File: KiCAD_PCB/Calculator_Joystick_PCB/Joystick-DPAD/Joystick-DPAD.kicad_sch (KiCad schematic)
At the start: 2 parts

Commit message: Updated Joystick PCB
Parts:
- gave numbers to parts that had none: 1
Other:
- moved on the sheet: JOY1A, JOY1B
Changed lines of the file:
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@@
     (title "Joystick & D-PAD Module")
   )
-  (wire (pts (xy 39.116 21.844) (xy 39.116 24.384))
+  (wire (pts (xy 28.956 27.432) (xy 28.956 29.972))
     (stroke (width 0) (type default) (color 0 0 0 0))
   )
-  (wire (pts (xy 44.45 51.562) (xy 46.99 51.562))
+  (wire (pts (xy 34.29 57.15) (xy 36.83 57.15))
     (stroke (width 0) (type default) (color 0 0 0 0))
   )
-  (wire (pts (xy 44.196 29.464) (xy 46.99 29.464))
+  (wire (pts (xy 34.036 35.052) (xy 36.83 35.052))
     (stroke (width 0) (type default) (color 0 0 0 0))
   )
-  (label "XOUT" (at 46.99 29.464 0)
+  (label "XOUT" (at 36.83 35.052 0)
     (effects (font (size 1.2446 1.2446)) (justify left bottom))
   )
-  (label "YOUT" (at 46.99 51.562 0)
+  (label "YOUT" (at 36.83 57.15 0)
     (effects (font (size 1.2446 1.2446)) (justify left bottom))
   )
-  (symbol (lib_id "Adafruit Mini Analog Thumbstick-eagle-import:GND") (at 39.116 37.084 0) (mirror y) (unit 1)
+  (symbol (lib_id "Adafruit Mini Analog Thumbstick-eagle-import:GND") (at 28.956 42.672 0) (mirror y) (unit 1)
     (in_bom yes) (on_board yes)
-    (property "Reference" "#GND?" (id 0) (at 39.116 37.084 0)
+    (property "Reference" "#GND0102" (id 0) (at 28.956 42.672 0)
       (effects (font (size 1.27 1.27)) hide)
     )
-    (property "Value" "GND" (id 1) (at 41.656 39.624 0)
+    (property "Value" "GND" (id 1) (at 31.496 45.212 0)
       (effects (font (size 1.778 1.5113)) (justify left bottom))
     )
-    (property "Footprint" "Adafruit Mini Analog Thumbstick:" (id 2) (at 39.116 37.084 0)
+    (property "Footprint" "Adafruit Mini Analog Thumbstick:" (id 2) (at 28.956 42.672 0)
       (effects (font (size 1.27 1.27)) hide)
     )
-    (property "Datasheet" "" (id 3) (at 39.116 37.084 0)
+    (property "Datasheet" "" (id 3) (at 28.956 42.672 0)
       (effects (font (size 1.27 1.27)) hide)
     )
     (pin "1")
   )
-  (symbol (lib_id "Adafruit Mini Analog Thumbstick-eagle-import:GND") (at 39.37 59.182 0) (mirror y) (unit 1)
+  (symbol (lib_id "Adafruit Mini Analog Thumbstick-eagle-import:GND") (at 29.21 64.77 0) (mirror y) (unit 1)
     (in_bom yes) (on_board yes)
-    (property "Reference" "#GND?" (id 0) (at 39.37 59.182 0)
+    (property "Reference" "#GND0101" (id 0) (at 29.21 64.77 0)
       (effects (font (size 1.27 1.27)) hide)
     )
-    (property "Value" "GND" (id 1) (at 41.91 61.722 0)
+    (property "Value" "GND" (id 1) (at 31.75 67.31 0)
       (effects (font (size 1.778 1.5113)) (justify left bottom))
     )
-    (property "Footprint" "Adafruit Mini Analog Thumbstick:" (id 2) (at 39.37 59.182 0)
+    (property "Footprint" "Adafruit Mini Analog Thumbstick:" (id 2) (at 29.21 64.77 0)
       (effects (font (size 1.27 1.27)) hide)
     )
-    (property "Datasheet" "" (id 3) (at 39.37 59.182 0)
+    (property "Datasheet" "" (id 3) (at 29.21 64.77 0)
       (effects (font (size 1.27 1.27)) hide)
     )
     (pin "1")
   )
-  (symbol (lib_id "Adafruit Mini Analog Thumbstick-eagle-import:JOYSTICK_ANALOG_XY") (at 39.116 29.464 0) (unit 1)
+  (symbol (lib_id "Adafruit Mini Analog Thumbstick-eagle-import:JOYSTICK_ANALOG_XY") (at 28.956 35.052 0) (unit 1)
     (in_bom yes) (on_board yes)
-    (property "Reference" "JOY?" (id 0) (at 33.147 33.274 90)
+    (property "Reference" "JOY1" (id 0) (at 22.987 38.862 90)
       (effects (font (size 1.27 1.0795)) (justify left bottom))
     )
-    (property "Value" "JOYSTICK_ANALOG_XY" (id 1) (at 35.306 33.274 90)
+    (property "Value" "JOYSTICK_ANALOG_XY" (id 1) (at 25.146 38.862 90)
       (effects (font (size 1.27 1.0795)) (justify left bottom))
     )
-    (property "Footprint" "Adafruit Mini Analog Thumbstick:JOYSTICK_ANALOG_MINITHM" (id 2) (at 39.116 29.464 0)
+    (property "Footprint" "Adafruit Mini Analog Thumbstick:JOYSTICK_ANALOG_MINITHM" (id 2) (at 28.956 35.052 0)
       (effects (font (size 1.27 1.27)) hide)
     )
-    (property "Datasheet" "" (id 3) (at 39.116 29.464 0)
+    (property "Datasheet" "" (id 3) (at 28.956 35.052 0)
       (effects (font (size 1.27 1.27)) hide)
     )
@@
     (pin "Y-")
   )
-  (symbol (lib_id "Adafruit Mini Analog Thumbstick-eagle-import:3.3V") (at 39.37 43.942 0) (unit 1)
+  (symbol (lib_id "Adafruit Mini Analog Thumbstick-eagle-import:3.3V") (at 29.21 49.53 0) (unit 1)
     (in_bom yes) (on_board yes)
-    (property "Reference" "#U$?" (id 0) (at 39.37 43.942 0)
+    (property "Reference" "#U$0101" (id 0) (at 29.21 49.53 0)
       (effects (font (size 1.27 1.27)) hide)
     )
-    (property "Value" "3.3V" (id 1) (at 37.846 42.926 0)
+    (property "Value" "3.3V" (id 1) (at 27.686 48.514 0)
       (effects (font (size 1.27 1.0795)) (justify left bottom))
     )
-    (property "Footprint" "Adafruit Mini Analog Thumbstick:" (id 2) (at 39.37 43.942 0)
+    (property "Footprint" "Adafruit Mini Analog Thumbstick:" (id 2) (at 29.21 49.53 0)
       (effects (font (size 1.27 1.27)) hide)
     )
-    (property "Datasheet" "" (id 3) (at 39.37 43.942 0)
+    (property "Datasheet" "" (id 3) (at 29.21 49.53 0)
       (effects (font (size 1.27 1.27)) hide)
     )
     (pin "1")
   )
-  (symbol (lib_id "Adafruit Mini Analog Thumbstick-eagle-import:JOYSTICK_ANALOG_XY") (at 39.37 51.562 0) (unit 2)
+  (symbol (lib_id "Adafruit Mini Analog Thumbstick-eagle-import:JOYSTICK_ANALOG_XY") (at 29.21 57.15 0) (unit 2)
     (in_bom yes) (on_board yes)
-    (property "Reference" "JOY?" (id 0) (at 33.401 55.372 90)
+    (property "Reference" "JOY1" (id 0) (at 23.241 60.96 90)
       (effects (font (size 1.27 1.0795)) (justify left bottom))
     )
-    (property "Value" "JOYSTICK_ANALOG_XY" (id 1) (at 35.56 55.372 90)
+    (property "Value" "JOYSTICK_ANALOG_XY" (id 1) (at 25.4 60.96 90)
       (effects (font (size 1.27 1.0795)) (justify left bottom))
     )
-    (property "Footprint" "Adafruit Mini Analog Thumbstick:JOYSTICK_ANALOG_MINITHM" (id 2) (at 39.37 51.562 0)
+    (property "Footprint" "Adafruit Mini Analog Thumbstick:JOYSTICK_ANALOG_MINITHM" (id 2) (at 29.21 57.15 0)
       (effects (font (size 1.27 1.27)) hide)
     )
-    (property "Datasheet" "" (id 3) (at 39.37 51.562 0)
+    (property "Datasheet" "" (id 3) (at 29.21 57.15 0)
       (effects (font (size 1.27 1.27)) hide)
     )
@@
     (pin "Y-")
   )
-  (symbol (lib_id "Adafruit Mini Analog Thumbstick-eagle-import:3.3V") (at 39.116 19.304 0) (unit 1)
+  (symbol (lib_id "Adafruit Mini Analog Thumbstick-eagle-import:3.3V") (at 28.956 24.892 0) (unit 1)
     (in_bom yes) (on_board yes)
-    (property "Reference" "#U$?" (id 0) (at 39.116 19.304 0)
+    (property "Reference" "#U$0102" (id 0) (at 28.956 24.892 0)
       (effects (font (size 1.27 1.27)) hide)
     )
-    (property "Value" "3.3V" (id 1) (at 37.592 18.288 0)
+    (property "Value" "3.3V" (id 1) (at 27.432 23.876 0)
       (effects (font (size 1.27 1.0795)) (justify left bottom))
     )
-    (property "Footprint" "Adafruit Mini Analog Thumbstick:" (id 2) (at 39.116 19.304 0)
+    (property "Footprint" "Adafruit Mini Analog Thumbstick:" (id 2) (at 28.956 24.892 0)
       (effects (font (size 1.27 1.27)) hide)
     )
-    (property "Datasheet" "" (id 3) (at 39.116 19.304 0)
+    (property "Datasheet" "" (id 3) (at 28.956 24.892 0)
       (effects (font (size 1.27 1.27)) hide)
     )
@@
   )
   (symbol_instances
+    (path "/172a6950-d4da-4136-ab6c-acd82359a76c"
+      (reference "#GND0101") (unit 1) (value "GND") (footprint "Adafruit Mini Analog Thumbstick:")
+    )
     (path "/0f12fe28-ff82-4f6f-ac3d-278eb8fd328e"
-      (reference "#GND?") (unit 1) (value "GND") (footprint "Adafruit Mini Analog Thumbstick:")
-    )
-    (path "/172a6950-d4da-4136-ab6c-acd82359a76c"
-      (reference "#GND?") (unit 1) (value "GND") (footprint "Adafruit Mini Analog Thumbstick:")
+      (reference "#GND0102") (unit 1) (value "GND") (footprint "Adafruit Mini Analog Thumbstick:")
     )
     (path "/66553eac-3edc-435c-bc67-3973452c2abb"
-      (reference "#U$?") (unit 1) (value "3.3V") (footprint "Adafruit Mini Analog Thumbstick:")
+      (reference "#U$0101") (unit 1) (value "3.3V") (footprint "Adafruit Mini Analog Thumbstick:")
     )
     (path "/f40b7176-bd86-42a6-95f2-24abfa99b611"
-      (reference "#U$?") (unit 1) (value "3.3V") (footprint "Adafruit Mini Analog Thumbstick:")
+      (reference "#U$0102") (unit 1) (value "3.3V") (footprint "Adafruit Mini Analog Thumbstick:")
     )
     (path "/3da07d8c-85c3-4a2f-a9bc-8b9585ef72db"
-      (reference "JOY?") (unit 1) (value "JOYSTICK_ANALOG_XY") (footprint "Adafruit Mini Analog Thumbstick:JOYSTICK_ANALOG_MINITHM")
+      (reference "JOY1") (unit 1) (value "JOYSTICK_ANALOG_XY") (footprint "Adafruit Mini Analog Thumbstick:JOYSTICK_ANALOG_MINITHM")
     )
     (path "/8108969a-3205-458d-b27a-a211d53ba7b0"
-      (reference "JOY?") (unit 2) (value "JOYSTICK_ANALOG_XY") (footprint "Adafruit Mini Analog Thumbstick:JOYSTICK_ANALOG_MINITHM")
+      (reference "JOY1") (unit 2) (value "JOYSTICK_ANALOG_XY") (footprint "Adafruit Mini Analog Thumbstick:JOYSTICK_ANALOG_MINITHM")
     )
   )

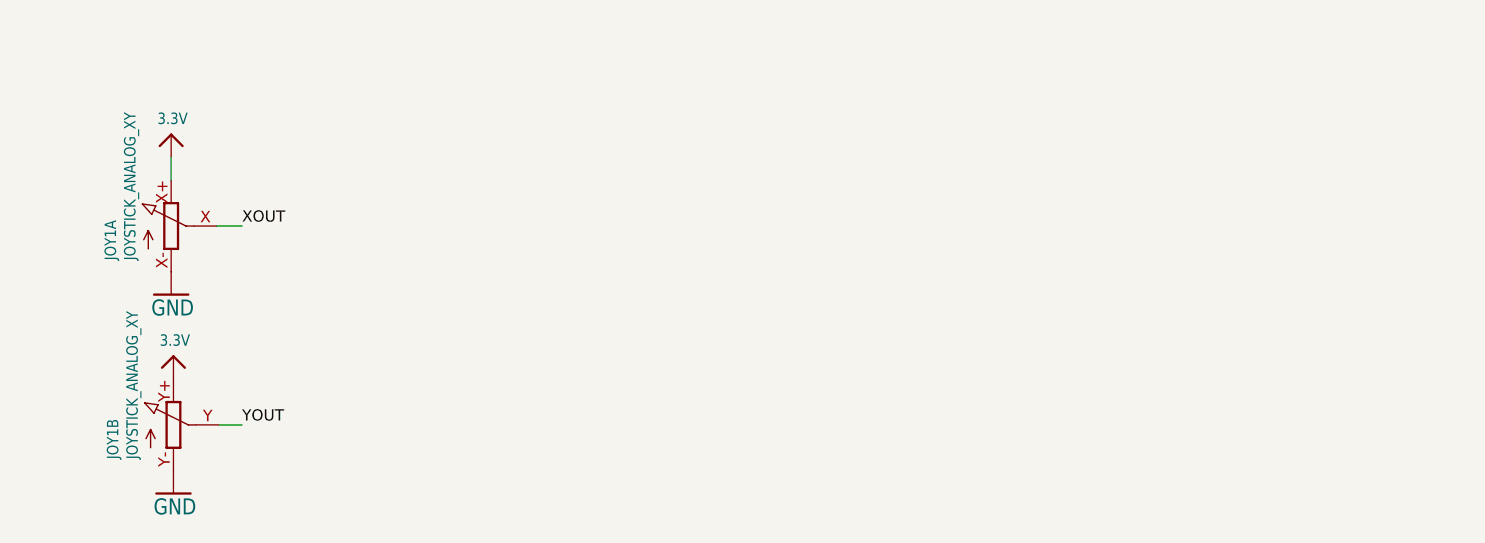
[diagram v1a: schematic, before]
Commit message: JoyStick PCB Updates
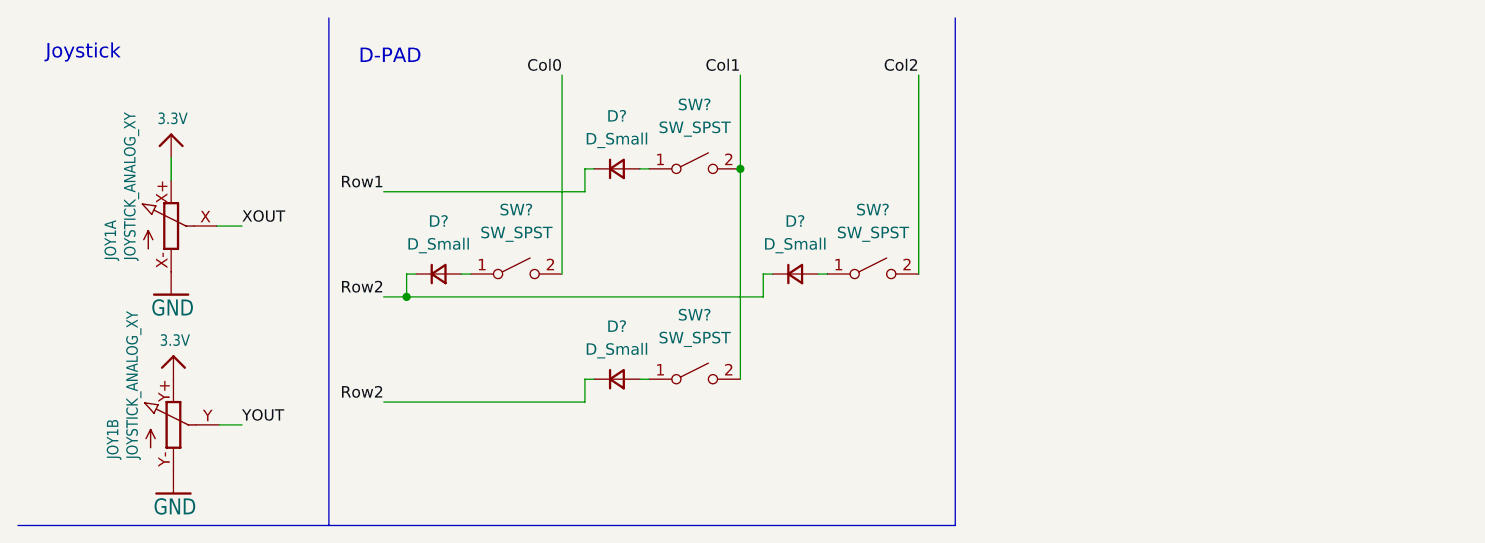
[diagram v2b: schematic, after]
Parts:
- added D? (x4): D_Small, Diode_SMD:D_SOD-123, symbol Device:D_Small
- added SW? (x4): SW_SPST, KSA1M331LFT_Footprint:KSA1M331LFT, symbol Switch:SW_SPST
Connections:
- new net: D?.2 (A), SW?.1 (A) (x4)
- new net Col0: SW?.2 (B)
- new net Col1: SW?.2 (B), SW?.2 (B)
- new net Col2: SW?.2 (B)
- new net Row1: D?.1 (K)
- new net Row2: D?.1 (K), D?.1 (K), D?.1 (K)
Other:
- note added: "D-PAD"
- note added: "Joystick"

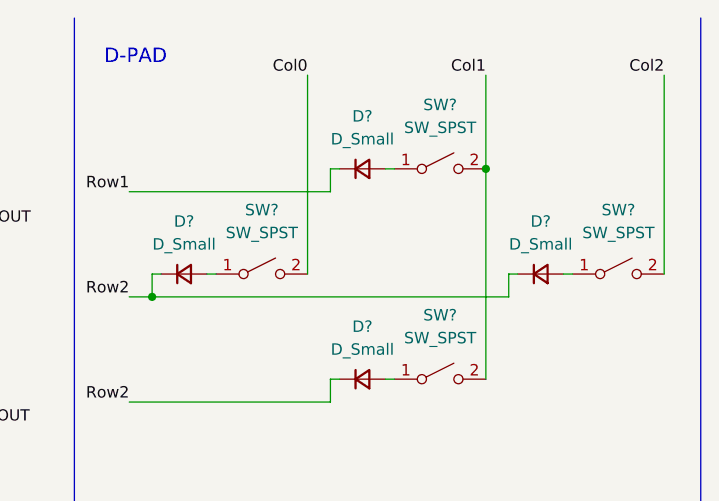
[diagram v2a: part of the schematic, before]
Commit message: JoyStick PCB Updates
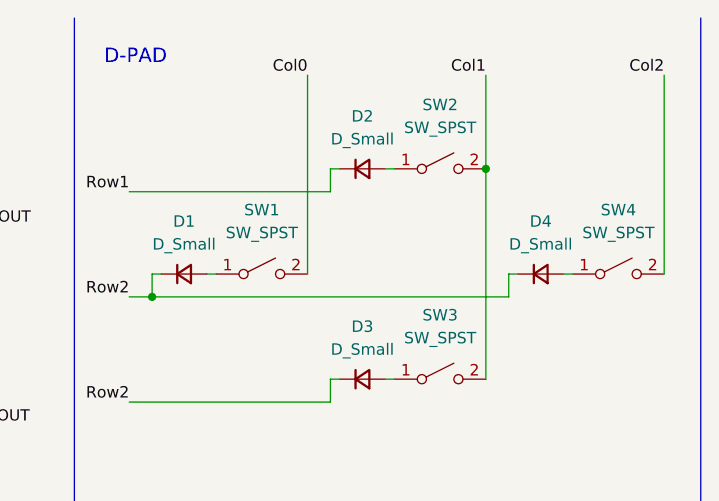
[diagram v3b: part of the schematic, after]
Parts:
- JOY1: footprint Adafruit Mini Analog Thumbstick:JOYSTICK_ANALOG_MINITHM -> (none)
- SW1, SW2, SW3, SW4: renamed from SW?; footprint KSA1M331LFT_Footprint:KSA1M331LFT -> (none)
- gave numbers to parts that had none: 4
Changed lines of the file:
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@@
   (symbol (lib_id "Switch:SW_SPST") (at 106.934 40.386 0) (unit 1)
     (in_bom yes) (on_board yes) (fields_autoplaced)
-    (property "Reference" "SW?" (id 0) (at 106.934 33.274 0))
+    (property "Reference" "SW4" (id 0) (at 106.934 33.274 0))
     (property "Value" "SW_SPST" (id 1) (at 106.934 35.814 0))
-    (property "Footprint" "KSA1M331LFT_Footprint:KSA1M331LFT" (id 2) (at 106.934 40.386 0)
+    (property "Footprint" "" (id 2) (at 106.934 40.386 0)
       (effects (font (size 1.27 1.27)) hide)
     )
@@
   (symbol (lib_id "Device:D_Small") (at 58.674 40.386 0) (unit 1)
     (in_bom yes) (on_board yes) (fields_autoplaced)
-    (property "Reference" "D?" (id 0) (at 58.674 34.544 0))
+    (property "Reference" "D1" (id 0) (at 58.674 34.544 0))
     (property "Value" "D_Small" (id 1) (at 58.674 37.084 0))
     (property "Footprint" "Diode_SMD:D_SOD-123" (id 2) (at 58.674 40.386 90)
@@
   (symbol (lib_id "Switch:SW_SPST") (at 87.122 52.07 0) (unit 1)
     (in_bom yes) (on_board yes) (fields_autoplaced)
-    (property "Reference" "SW?" (id 0) (at 87.122 44.958 0))
+    (property "Reference" "SW3" (id 0) (at 87.122 44.958 0))
     (property "Value" "SW_SPST" (id 1) (at 87.122 47.498 0))
-    (property "Footprint" "KSA1M331LFT_Footprint:KSA1M331LFT" (id 2) (at 87.122 52.07 0)
+    (property "Footprint" "" (id 2) (at 87.122 52.07 0)
       (effects (font (size 1.27 1.27)) hide)
     )
@@
   (symbol (lib_id "Device:D_Small") (at 78.486 52.07 0) (unit 1)
     (in_bom yes) (on_board yes) (fields_autoplaced)
-    (property "Reference" "D?" (id 0) (at 78.486 46.228 0))
+    (property "Reference" "D3" (id 0) (at 78.486 46.228 0))
     (property "Value" "D_Small" (id 1) (at 78.486 48.768 0))
     (property "Footprint" "Diode_SMD:D_SOD-123" (id 2) (at 78.486 52.07 90)
@@
       (effects (font (size 1.27 1.0795)) (justify left bottom))
     )
-    (property "Footprint" "Adafruit Mini Analog Thumbstick:JOYSTICK_ANALOG_MINITHM" (id 2) (at 28.956 35.052 0)
+    (property "Footprint" "" (id 2) (at 28.956 35.052 0)
       (effects (font (size 1.27 1.27)) hide)
     )
@@
   (symbol (lib_id "Switch:SW_SPST") (at 87.122 28.702 0) (unit 1)
     (in_bom yes) (on_board yes) (fields_autoplaced)
-    (property "Reference" "SW?" (id 0) (at 87.122 21.59 0))
+    (property "Reference" "SW2" (id 0) (at 87.122 21.59 0))
     (property "Value" "SW_SPST" (id 1) (at 87.122 24.13 0))
-    (property "Footprint" "KSA1M331LFT_Footprint:KSA1M331LFT" (id 2) (at 87.122 28.702 0)
+    (property "Footprint" "" (id 2) (at 87.122 28.702 0)
       (effects (font (size 1.27 1.27)) hide)
     )
@@
       (effects (font (size 1.27 1.0795)) (justify left bottom))
     )
-    (property "Footprint" "Adafruit Mini Analog Thumbstick:JOYSTICK_ANALOG_MINITHM" (id 2) (at 29.21 57.15 0)
+    (property "Footprint" "" (id 2) (at 29.21 57.15 0)
       (effects (font (size 1.27 1.27)) hide)
     )
@@
   (symbol (lib_id "Switch:SW_SPST") (at 67.31 40.386 0) (unit 1)
     (in_bom yes) (on_board yes) (fields_autoplaced)
-    (property "Reference" "SW?" (id 0) (at 67.31 33.274 0))
+    (property "Reference" "SW1" (id 0) (at 67.31 33.274 0))
     (property "Value" "SW_SPST" (id 1) (at 67.31 35.814 0))
-    (property "Footprint" "KSA1M331LFT_Footprint:KSA1M331LFT" (id 2) (at 67.31 40.386 0)
+    (property "Footprint" "" (id 2) (at 67.31 40.386 0)
       (effects (font (size 1.27 1.27)) hide)
     )
@@
   (symbol (lib_id "Device:D_Small") (at 78.486 28.702 0) (unit 1)
     (in_bom yes) (on_board yes) (fields_autoplaced)
-    (property "Reference" "D?" (id 0) (at 78.486 22.86 0))
+    (property "Reference" "D2" (id 0) (at 78.486 22.86 0))
     (property "Value" "D_Small" (id 1) (at 78.486 25.4 0))
     (property "Footprint" "Diode_SMD:D_SOD-123" (id 2) (at 78.486 28.702 90)
@@
   (symbol (lib_id "Device:D_Small") (at 98.298 40.386 0) (unit 1)
     (in_bom yes) (on_board yes) (fields_autoplaced)
-    (property "Reference" "D?" (id 0) (at 98.298 34.544 0))
+    (property "Reference" "D4" (id 0) (at 98.298 34.544 0))
     (property "Value" "D_Small" (id 1) (at 98.298 37.084 0))
     (property "Footprint" "Diode_SMD:D_SOD-123" (id 2) (at 98.298 40.386 90)
@@
     )
     (path "/220ac994-5d59-4456-966f-367fff35b973"
-      (reference "D?") (unit 1) (value "D_Small") (footprint "Diode_SMD:D_SOD-123")
+      (reference "D1") (unit 1) (value "D_Small") (footprint "Diode_SMD:D_SOD-123")
+    )
+    (path "/ab5dcf3b-7b8d-4e3b-b68a-dff46c10b43e"
+      (reference "D2") (unit 1) (value "D_Small") (footprint "Diode_SMD:D_SOD-123")
     )
     (path "/34260486-9d16-4d32-aabe-ee160836930b"
-      (reference "D?") (unit 1) (value "D_Small") (footprint "Diode_SMD:D_SOD-123")
-    )
-    (path "/ab5dcf3b-7b8d-4e3b-b68a-dff46c10b43e"
-      (reference "D?") (unit 1) (value "D_Small") (footprint "Diode_SMD:D_SOD-123")
+      (reference "D3") (unit 1) (value "D_Small") (footprint "Diode_SMD:D_SOD-123")
     )
     (path "/f5b1db93-cb0e-4f6b-bd1a-6ac9c1b58c5a"
-      (reference "D?") (unit 1) (value "D_Small") (footprint "Diode_SMD:D_SOD-123")
+      (reference "D4") (unit 1) (value "D_Small") (footprint "Diode_SMD:D_SOD-123")
     )
     (path "/3da07d8c-85c3-4a2f-a9bc-8b9585ef72db"
-      (reference "JOY1") (unit 1) (value "JOYSTICK_ANALOG_XY") (footprint "Adafruit Mini Analog Thumbstick:JOYSTICK_ANALOG_MINITHM")
+      (reference "JOY1") (unit 1) (value "JOYSTICK_ANALOG_XY") (footprint "Adafruit_Thumbstick:JOYSTICK_ANALOG_MINITHM")
     )
     (path "/8108969a-3205-458d-b27a-a211d53ba7b0"
-      (reference "JOY1") (unit 2) (value "JOYSTICK_ANALOG_XY") (footprint "Adafruit Mini Analog Thumbstick:JOYSTICK_ANALOG_MINITHM")
+      (reference "JOY1") (unit 2) (value "JOYSTICK_ANALOG_XY") (footprint "Adafruit_Thumbstick:JOYSTICK_ANALOG_MINITHM")
+    )
+    (path "/9d72fa1e-2c75-4e9b-be14-33187cf8983c"
+      (reference "SW1") (unit 1) (value "SW_SPST") (footprint "KSA_Switch:KSA1M331LFT")
+    )
+    (path "/8105b584-22ed-40dc-ab76-823e721e7a31"
+      (reference "SW2") (unit 1) (value "SW_SPST") (footprint "KSA_Switch:KSA1M331LFT")
+    )
+    (path "/28aac413-f452-42d6-bc18-e7b9fbf4044c"
+      (reference "SW3") (unit 1) (value "SW_SPST") (footprint "KSA_Switch:KSA1M331LFT")
     )
     (path "/21e6c13a-79b6-4465-b176-eb66598a4f1e"
-      (reference "SW?") (unit 1) (value "SW_SPST") (footprint "KSA1M331LFT_Footprint:KSA1M331LFT")
-    )
-    (path "/28aac413-f452-42d6-bc18-e7b9fbf4044c"
-      (reference "SW?") (unit 1) (value "SW_SPST") (footprint "KSA1M331LFT_Footprint:KSA1M331LFT")
-    )
-    (path "/8105b584-22ed-40dc-ab76-823e721e7a31"
-      (reference "SW?") (unit 1) (value "SW_SPST") (footprint "KSA1M331LFT_Footprint:KSA1M331LFT")
-    )
-    (path "/9d72fa1e-2c75-4e9b-be14-33187cf8983c"
-      (reference "SW?") (unit 1) (value "SW_SPST") (footprint "KSA1M331LFT_Footprint:KSA1M331LFT")
-    )
-  )
+      (reference "SW4") (unit 1) (value "SW_SPST") (footprint "KSA_Switch:KSA1M331LFT")
+    )
+  )
